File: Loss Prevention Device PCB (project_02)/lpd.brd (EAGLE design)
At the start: 160 x 100 mm, 5 parts, among them K1 LPPB041NGCN-RC, U1 POCKETBEAGLE, U2 GT-U7, U3 HM-10

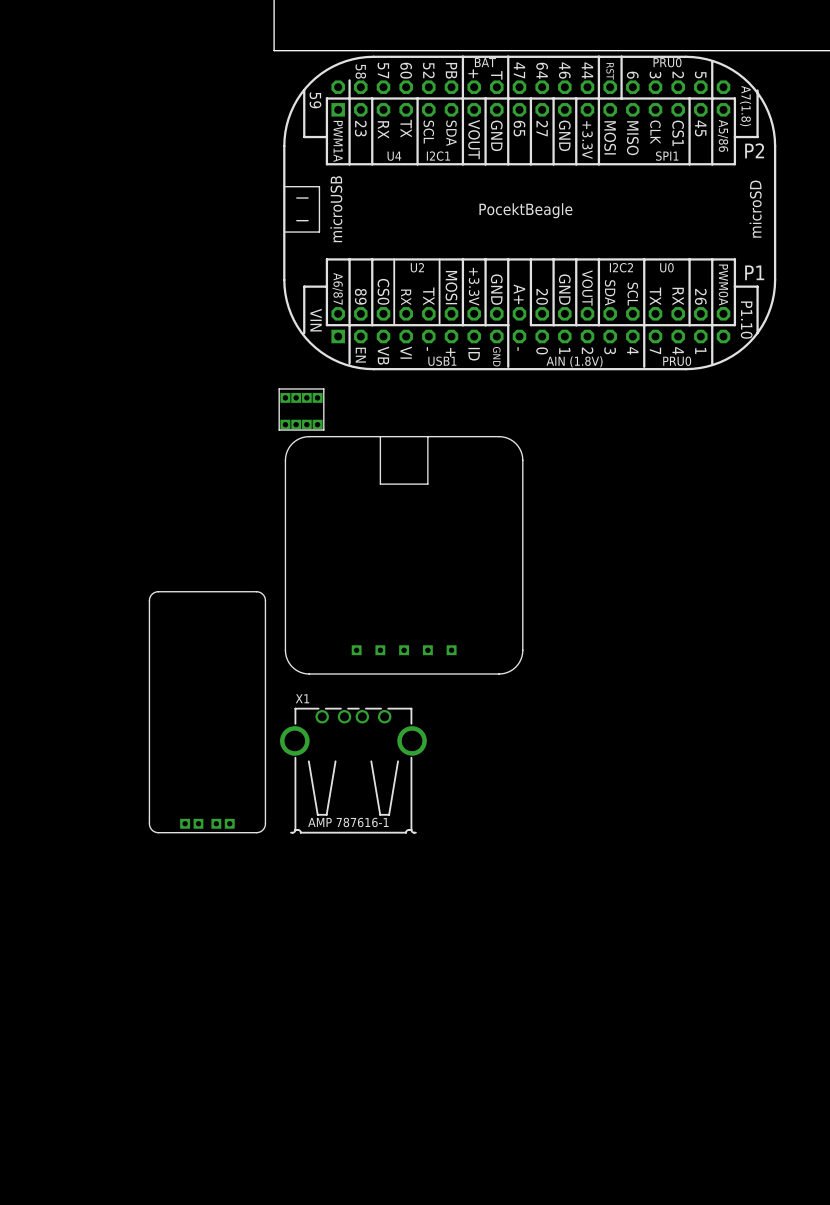
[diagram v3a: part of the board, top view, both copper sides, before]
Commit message: Split pocketbeagle symbol into 2
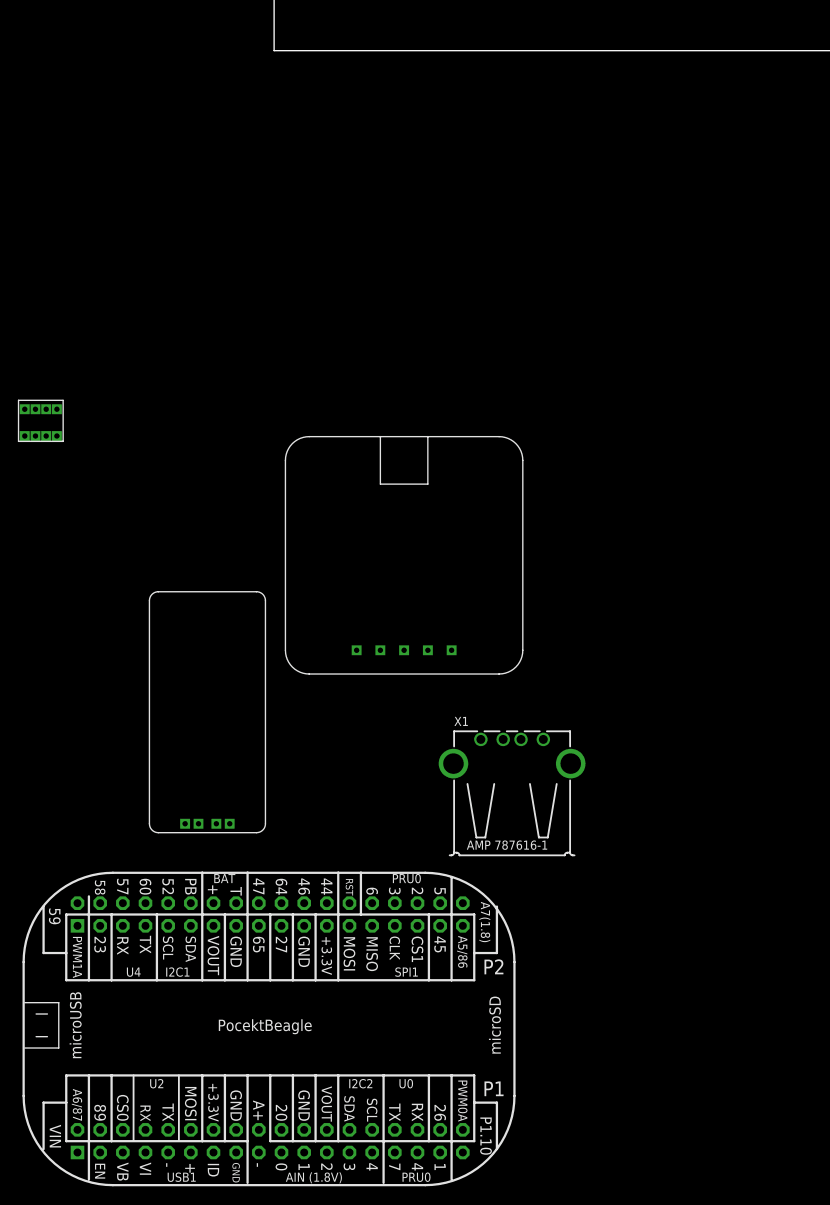
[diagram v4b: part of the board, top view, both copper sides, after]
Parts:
- removed U1: POCKETBEAGLE, lpd:POCKETBEAGLE
- added U$1: POCKETBEAGLE, lpd:POCKETBEAGLE
- moved K1 29.2 mm to (-27.9, -43.2)
- moved X1 18.0 mm to (26.7, -90.2)
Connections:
- removed net USB1.GND: X1.4
- net BAT.VIN: now also U$1.P1_12; no longer U1.P2_14
- net GND: now also U$1.P2_22, U$1.P2_23, U$1.P2_24, U$1.P2_25, U$1.P2_26, X1.4; no longer U1.P1_15, U1.P1_16, U1.P1_22, U1.P2_15, U1.P2_21
- net UART2.RX: now also U$1.P2_27; no longer U1.P1_08
- net UART2.TX: now also U$1.P2_28; no longer U1.P1_10
- net UART4.RX: now also U$1.P2_29; no longer U1.P2_05
- net UART4.TX: now also U$1.P2_30; no longer U1.P2_07
- net USB1.D+: now also U$1.P2_31; no longer U1.P1_11
- net USB1.D-: now also U$1.P2_32; no longer U1.P1_09
- net USB1.VBUS: now also U$1.P2_35; no longer U1.P1_05
- net VDD_3P3V: now also U$1.P2_20, U$1.P2_21; no longer U1.P1_14, U1.P2_23
- net VIN: now also U$1.P2_17; no longer U1.P1_01
- net VOUT: now also U$1.P2_18, U$1.P2_19; no longer U1.P1_24, U1.P2_13
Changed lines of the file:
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@@
 </autorouter>
 <elements>
-<element name="U1" library="lpd" package="POCKETBEAGLE" value="POCKETBEAGLE" x="1.27" y="-35.56" smashed="yes"/>
-<element name="K1" library="lpd" package="FEMALE90" value="LPPB041NGCN-RC" x="1.27" y="-41.91" smashed="yes"/>
+<element name="K1" library="lpd" package="FEMALE90" value="LPPB041NGCN-RC" x="-27.94" y="-43.18" smashed="yes"/>
 <element name="U2" library="lpd" package="GPS" value="GT-U7" x="1.27" y="-69.85" smashed="yes"/>
-<element name="X1" library="lpd" package="GHI2_USB_HOST_HORIZONTAL_W/CHASSIS_GND" value="" x="8.89" y="-87.63" smashed="yes">
-<attribute name="NAME" x="2.3899" y="-73.1299" size="1.016" layer="25" ratio="12"/>
-<attribute name="VALUE" x="4.3899" y="-77.63" size="1.016" layer="27" ratio="12"/>
+<element name="X1" library="lpd" package="GHI2_USB_HOST_HORIZONTAL_W/CHASSIS_GND" value="" x="26.67" y="-90.17" smashed="yes">
+<attribute name="NAME" x="20.1699" y="-75.6699" size="1.016" layer="25" ratio="12"/>
+<attribute name="VALUE" x="22.1699" y="-80.17" size="1.016" layer="27" ratio="12"/>
 </element>
 <element name="U3" library="lpd" package="BT" value="HM-10" x="-13.97" y="-87.63" smashed="yes"/>
+<element name="U$1" library="lpd" package="POCKETBEAGLE" value="POCKETBEAGLE" x="-27.94" y="-127" smashed="yes"/>
 </elements>
 <signals>
-<signal name="VIN">
-<contactref element="U1" pad="P1_01"/>
-</signal>
 <signal name="GND">
-<contactref element="U1" pad="P1_22"/>
-<contactref element="U1" pad="P2_21"/>
 <contactref element="U2" pad="P$1"/>
 <contactref element="K1" pad="P$2"/>
-<contactref element="U1" pad="P1_15"/>
-<contactref element="U1" pad="P1_16"/>
-<contactref element="U1" pad="P2_15"/>
-<wire x1="2.47" y1="-41.91" x2="9.25" y2="-67.19" width="0" layer="19" extent="1-1"/>
-<wire x1="24.96" y1="-32.03" x2="2.47" y2="-41.91" width="0" layer="19" extent="1-1"/>
-<wire x1="24.96" y1="-29.49" x2="24.96" y2="-32.03" width="0" layer="19" extent="1-1"/>
-<wire x1="32.58" y1="-29.49" x2="24.96" y2="-29.49" width="0" layer="19" extent="1-1"/>
-<wire x1="32.58" y1="-6.63" x2="32.58" y2="-29.49" width="0" layer="19" extent="1-1"/>
-<wire x1="24.96" y1="-6.63" x2="32.58" y2="-6.63" width="0" layer="19" extent="1-1"/>
-</signal>
-<signal name="VOUT">
-<contactref element="U1" pad="P1_24"/>
-<contactref element="U1" pad="P2_13"/>
-<wire x1="35.12" y1="-29.49" x2="22.42" y2="-6.63" width="0" layer="19" extent="1-1"/>
-</signal>
-<signal name="BAT.VIN">
-<contactref element="U1" pad="P2_14"/>
+<contactref element="X1" pad="4"/>
+<contactref element="U$1" pad="P2_23"/>
+<contactref element="U$1" pad="P2_24"/>
+<contactref element="U$1" pad="P2_25"/>
+<contactref element="U$1" pad="P2_26"/>
+<contactref element="U$1" pad="P2_22"/>
+<wire x1="5.91" y1="-95.53" x2="5.91" y2="-98.07" width="0" layer="19" extent="1-1"/>
+<wire x1="3.37" y1="-95.53" x2="5.91" y2="-95.53" width="0" layer="19" extent="1-1"/>
+<wire x1="8.45" y1="-98.07" x2="5.91" y2="-98.07" width="0" layer="19" extent="1-1"/>
+<wire x1="8.45" y1="-95.53" x2="5.91" y2="-95.53" width="0" layer="19" extent="1-1"/>
+<wire x1="9.25" y1="-67.19" x2="8.45" y2="-95.53" width="0" layer="19" extent="1-1"/>
+<wire x1="30.17" y1="-77.18" x2="9.25" y2="-67.19" width="0" layer="19" extent="1-1"/>
+<wire x1="-26.74" y1="-43.18" x2="9.25" y2="-67.19" width="0" layer="19" extent="1-1"/>
 </signal>
 <signal name="VDD_3P3V">
-<contactref element="U1" pad="P2_23"/>
-<contactref element="U1" pad="P1_14"/>
 <contactref element="U2" pad="P$5"/>
 <contactref element="K1" pad="P$1"/>
-<wire x1="1.27" y1="-41.91" x2="19.89" y2="-67.19" width="0" layer="19" extent="1-1"/>
-<wire x1="22.42" y1="-29.49" x2="1.27" y2="-41.91" width="0" layer="19" extent="1-1"/>
-<wire x1="35.12" y1="-6.63" x2="22.42" y2="-29.49" width="0" layer="19" extent="1-1"/>
+<contactref element="U$1" pad="P2_21"/>
+<contactref element="U$1" pad="P2_20"/>
+<wire x1="0.83" y1="-95.53" x2="3.37" y2="-98.07" width="0" layer="19" extent="1-1"/>
+<wire x1="19.89" y1="-67.19" x2="0.83" y2="-95.53" width="0" layer="19" extent="1-1"/>
+<wire x1="-27.94" y1="-43.18" x2="19.89" y2="-67.19" width="0" layer="19" extent="1-1"/>
 </signal>
 <signal name="UART2.RX">
 <contactref element="U2" pad="P$3"/>
-<contactref element="U1" pad="P1_08"/>
-<wire x1="14.8" y1="-29.49" x2="14.57" y2="-67.19" width="0" layer="19" extent="1-1"/>
+<contactref element="U$1" pad="P2_27"/>
+<wire x1="14.57" y1="-67.19" x2="10.99" y2="-98.07" width="0" layer="19" extent="1-1"/>
 </signal>
 <signal name="UART2.TX">
 <contactref element="U2" pad="P$4"/>
-<contactref element="U1" pad="P1_10"/>
-<wire x1="17.34" y1="-29.49" x2="17.23" y2="-67.19" width="0" layer="19" extent="1-1"/>
+<contactref element="U$1" pad="P2_28"/>
+<wire x1="17.23" y1="-67.19" x2="10.99" y2="-95.53" width="0" layer="19" extent="1-1"/>
 </signal>
 <signal name="UART4.TX">
 <contactref element="K1" pad="P$3"/>
-<contactref element="U1" pad="P2_07"/>
-<wire x1="14.8" y1="-6.63" x2="3.67" y2="-41.91" width="0" layer="19" extent="1-1"/>
+<contactref element="U$1" pad="P2_30"/>
+<wire x1="-25.54" y1="-43.18" x2="13.53" y2="-95.53" width="0" layer="19" extent="1-1"/>
 </signal>
 <signal name="UART4.RX">
 <contactref element="K1" pad="P$4"/>
-<contactref element="U1" pad="P2_05"/>
-<wire x1="12.26" y1="-6.63" x2="4.87" y2="-41.91" width="0" layer="19" extent="1-1"/>
+<contactref element="U$1" pad="P2_29"/>
+<wire x1="-24.34" y1="-43.18" x2="13.53" y2="-98.07" width="0" layer="19" extent="1-1"/>
 </signal>
 <signal name="ANGLE1">
 <contactref element="K1" pad="P$5"/>
 <contactref element="U3" pad="P$4"/>
-<wire x1="1.27" y1="-38.91" x2="-4.97" y2="-86.63" width="0" layer="19" extent="1-1"/>
+<wire x1="-27.94" y1="-40.18" x2="-4.97" y2="-86.63" width="0" layer="19" extent="1-1"/>
 </signal>
 <signal name="ANGLE2">
 <contactref element="K1" pad="P$6"/>
 <contactref element="U3" pad="P$1"/>
-<wire x1="2.47" y1="-38.91" x2="-9.97" y2="-86.63" width="0" layer="19" extent="1-1"/>
+<wire x1="-26.74" y1="-40.18" x2="-9.97" y2="-86.63" width="0" layer="19" extent="1-1"/>
 </signal>
 <signal name="ANGLE3">
 <contactref element="K1" pad="P$7"/>
 <contactref element="U3" pad="P$3"/>
-<wire x1="3.67" y1="-38.91" x2="-6.47" y2="-86.63" width="0" layer="19" extent="1-1"/>
+<wire x1="-25.54" y1="-40.18" x2="-6.47" y2="-86.63" width="0" layer="19" extent="1-1"/>
 </signal>
 <signal name="ANGLE4">
 <contactref element="K1" pad="P$8"/>
 <contactref element="U3" pad="P$2"/>
-<wire x1="4.87" y1="-38.91" x2="-8.47" y2="-86.63" width="0" layer="19" extent="1-1"/>
+<wire x1="-24.34" y1="-40.18" x2="-8.47" y2="-86.63" width="0" layer="19" extent="1-1"/>
 </signal>
 <signal name="CGND">
 <contactref element="X1" pad="5"/>
 <contactref element="X1" pad="6"/>
-<wire x1="15.46" y1="-77.3501" x2="2.32" y2="-77.3501" width="0" layer="19" extent="1-1"/>
+<wire x1="33.24" y1="-79.8901" x2="20.1" y2="-79.8901" width="0" layer="19" extent="1-1"/>
 </signal>
 <signal name="USB1.VBUS">
 <contactref element="X1" pad="1"/>
-<contactref element="U1" pad="P1_05"/>
-<wire x1="12.26" y1="-32.03" x2="5.39" y2="-74.64" width="0" layer="19" extent="1-1"/>
+<contactref element="U$1" pad="P2_35"/>
+<wire x1="23.17" y1="-77.18" x2="21.15" y2="-98.07" width="0" layer="19" extent="1-1"/>
 </signal>
 <signal name="USB1.D-">
 <contactref element="X1" pad="2"/>
-<contactref element="U1" pad="P1_09"/>
-<wire x1="17.34" y1="-32.03" x2="7.89" y2="-74.64" width="0" layer="19" extent="1-1"/>
+<contactref element="U$1" pad="P2_32"/>
+<wire x1="25.67" y1="-77.18" x2="16.07" y2="-95.53" width="0" layer="19" extent="1-1"/>
 </signal>
 <signal name="USB1.D+">
 <contactref element="X1" pad="3"/>
-<contactref element="U1" pad="P1_11"/>
-<wire x1="19.88" y1="-32.03" x2="9.89" y2="-74.64" width="0" layer="19" extent="1-1"/>
+<contactref element="U$1" pad="P2_31"/>
+<wire x1="27.67" y1="-77.18" x2="16.07" y2="-98.07" width="0" layer="19" extent="1-1"/>
 </signal>
-<signal name="USB1.GND">
-<contactref element="X1" pad="4"/>
+<signal name="VIN">
+<contactref element="U$1" pad="P2_17"/>
+</signal>
+<signal name="VOUT">
+<contactref element="U$1" pad="P2_18"/>
+<contactref element="U$1" pad="P2_19"/>
+<wire x1="-1.71" y1="-95.53" x2="0.83" y2="-98.07" width="0" layer="19" extent="1-1"/>
+</signal>
+<signal name="BAT.VIN">
+<contactref element="U$1" pad="P1_12"/>
 </signal>
 </signals>

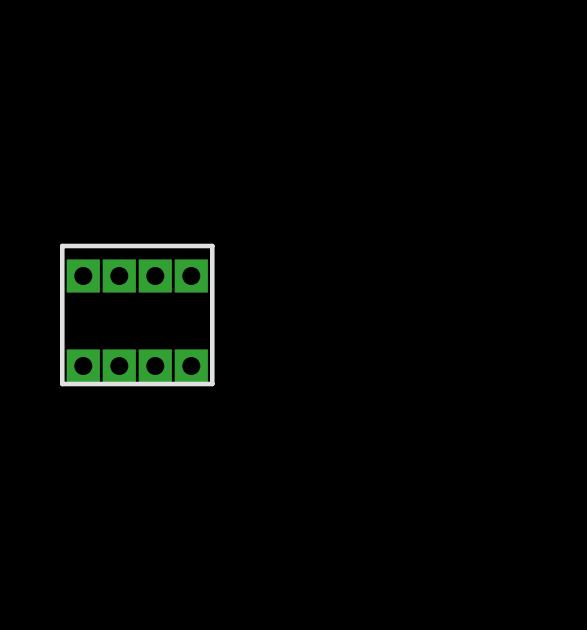
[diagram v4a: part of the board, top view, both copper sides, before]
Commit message: Removed 90 degree header and updated footprints
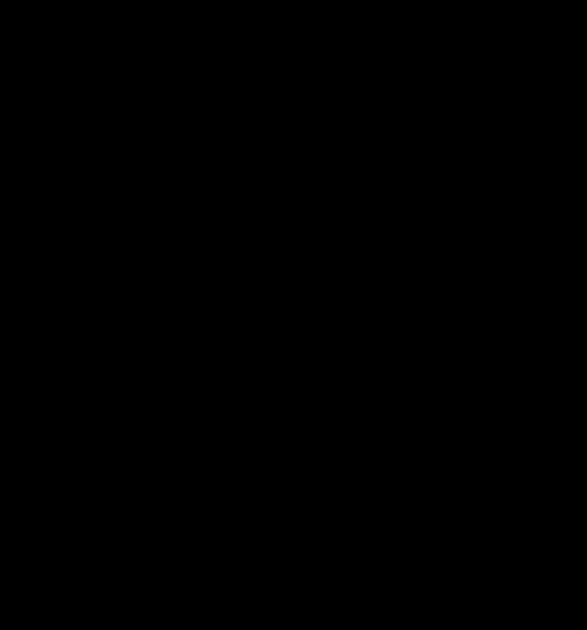
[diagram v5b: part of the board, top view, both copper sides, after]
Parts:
- removed K1: LPPB041NGCN-RC, lpd:FEMALE90
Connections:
- removed net ANGLE1: K1.P$5, U3.P$4
- removed net ANGLE2: K1.P$6, U3.P$1
- removed net ANGLE3: K1.P$7, U3.P$3
- removed net ANGLE4: K1.P$8, U3.P$2
- net GND: now also U3.P$1; no longer K1.P$2
- net UART4.RX: now also U3.P$2; no longer K1.P$4
- net UART4.TX: now also U3.P$3; no longer K1.P$3
- net VDD_3P3V: now also U3.P$4; no longer K1.P$1
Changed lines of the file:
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@@
 </autorouter>
 <elements>
-<element name="K1" library="lpd" package="FEMALE90" value="LPPB041NGCN-RC" x="-27.94" y="-43.18" smashed="yes"/>
 <element name="U2" library="lpd" package="GPS" value="GT-U7" x="1.27" y="-69.85" smashed="yes"/>
 <element name="X1" library="lpd" package="GHI2_USB_HOST_HORIZONTAL_W/CHASSIS_GND" value="" x="26.67" y="-90.17" smashed="yes">
@@
 <signal name="GND">
 <contactref element="U2" pad="P$1"/>
-<contactref element="K1" pad="P$2"/>
 <contactref element="X1" pad="4"/>
 <contactref element="U$1" pad="P2_23"/>
@@
 <contactref element="U$1" pad="P2_26"/>
 <contactref element="U$1" pad="P2_22"/>
-<wire x1="5.91" y1="-95.53" x2="5.91" y2="-98.07" width="0" layer="19" extent="1-1"/>
-<wire x1="3.37" y1="-95.53" x2="5.91" y2="-95.53" width="0" layer="19" extent="1-1"/>
+<contactref element="U3" pad="P$1"/>
+<wire x1="3.37" y1="-95.53" x2="-9.97" y2="-86.63" width="0" layer="19" extent="1-1"/>
+<wire x1="5.91" y1="-95.53" x2="3.37" y2="-95.53" width="0" layer="19" extent="1-1"/>
+<wire x1="5.91" y1="-98.07" x2="5.91" y2="-95.53" width="0" layer="19" extent="1-1"/>
 <wire x1="8.45" y1="-98.07" x2="5.91" y2="-98.07" width="0" layer="19" extent="1-1"/>
 <wire x1="8.45" y1="-95.53" x2="5.91" y2="-95.53" width="0" layer="19" extent="1-1"/>
-<wire x1="9.25" y1="-67.19" x2="8.45" y2="-95.53" width="0" layer="19" extent="1-1"/>
+<wire x1="9.25" y1="-67.19" x2="-9.97" y2="-86.63" width="0" layer="19" extent="1-1"/>
 <wire x1="30.17" y1="-77.18" x2="9.25" y2="-67.19" width="0" layer="19" extent="1-1"/>
-<wire x1="-26.74" y1="-43.18" x2="9.25" y2="-67.19" width="0" layer="19" extent="1-1"/>
 </signal>
 <signal name="VDD_3P3V">
 <contactref element="U2" pad="P$5"/>
-<contactref element="K1" pad="P$1"/>
 <contactref element="U$1" pad="P2_21"/>
 <contactref element="U$1" pad="P2_20"/>
+<contactref element="U3" pad="P$4"/>
 <wire x1="0.83" y1="-95.53" x2="3.37" y2="-98.07" width="0" layer="19" extent="1-1"/>
-<wire x1="19.89" y1="-67.19" x2="0.83" y2="-95.53" width="0" layer="19" extent="1-1"/>
-<wire x1="-27.94" y1="-43.18" x2="19.89" y2="-67.19" width="0" layer="19" extent="1-1"/>
+<wire x1="-4.97" y1="-86.63" x2="0.83" y2="-95.53" width="0" layer="19" extent="1-1"/>
+<wire x1="19.89" y1="-67.19" x2="-4.97" y2="-86.63" width="0" layer="19" extent="1-1"/>
 </signal>
 <signal name="UART2.RX">
@@
 </signal>
 <signal name="UART4.TX">
-<contactref element="K1" pad="P$3"/>
 <contactref element="U$1" pad="P2_30"/>
-<wire x1="-25.54" y1="-43.18" x2="13.53" y2="-95.53" width="0" layer="19" extent="1-1"/>
+<contactref element="U3" pad="P$3"/>
+<wire x1="13.53" y1="-95.53" x2="-6.47" y2="-86.63" width="0" layer="19" extent="1-1"/>
 </signal>
 <signal name="UART4.RX">
-<contactref element="K1" pad="P$4"/>
 <contactref element="U$1" pad="P2_29"/>
-<wire x1="-24.34" y1="-43.18" x2="13.53" y2="-98.07" width="0" layer="19" extent="1-1"/>
-</signal>
-<signal name="ANGLE1">
-<contactref element="K1" pad="P$5"/>
-<contactref element="U3" pad="P$4"/>
-<wire x1="-27.94" y1="-40.18" x2="-4.97" y2="-86.63" width="0" layer="19" extent="1-1"/>
-</signal>
-<signal name="ANGLE2">
-<contactref element="K1" pad="P$6"/>
-<contactref element="U3" pad="P$1"/>
-<wire x1="-26.74" y1="-40.18" x2="-9.97" y2="-86.63" width="0" layer="19" extent="1-1"/>
-</signal>
-<signal name="ANGLE3">
-<contactref element="K1" pad="P$7"/>
-<contactref element="U3" pad="P$3"/>
-<wire x1="-25.54" y1="-40.18" x2="-6.47" y2="-86.63" width="0" layer="19" extent="1-1"/>
-</signal>
-<signal name="ANGLE4">
-<contactref element="K1" pad="P$8"/>
 <contactref element="U3" pad="P$2"/>
-<wire x1="-24.34" y1="-40.18" x2="-8.47" y2="-86.63" width="0" layer="19" extent="1-1"/>
+<wire x1="13.53" y1="-98.07" x2="-8.47" y2="-86.63" width="0" layer="19" extent="1-1"/>
 </signal>
 <signal name="CGND">

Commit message: Board Placement Complete
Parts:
- moved U$1 144.3 mm to (38.1, 1.27), turned to 90 degrees
- moved U3 102.2 mm to (31.8, 3.81)
- moved U2 101.6 mm to (2.54, 31.8)
- moved X1 91.7 mm to (20.3, 1.27)
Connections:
- net BAT.VIN: now also U$1.P1_25; no longer U$1.P1_12
- net GND: now also U$1.P1_15, U$1.P1_16, U$1.P1_22, U$1.P2_15, U$1.P2_21; no longer U$1.P2_22, U$1.P2_23, U$1.P2_24, U$1.P2_25, U$1.P2_26
- net UART2.RX: now also U$1.P1_08; no longer U$1.P2_27
- net UART2.TX: now also U$1.P1_10; no longer U$1.P2_28
- net UART4.RX: now also U$1.P2_05; no longer U$1.P2_29
- net UART4.TX: now also U$1.P2_07; no longer U$1.P2_30
- net USB1.D+: now also U$1.P1_11; no longer U$1.P2_31
- net USB1.D-: now also U$1.P1_09; no longer U$1.P2_32
- net USB1.VBUS: now also U$1.P1_05; no longer U$1.P2_35
- net VDD_3P3V: now also U$1.P1_14, U$1.P1_23; no longer U$1.P2_20, U$1.P2_21
- net VIN: now also U$1.P2_34; no longer U$1.P2_17
- net VOUT: now also U$1.P2_35, U$1.P2_36; no longer U$1.P2_18, U$1.P2_19
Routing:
- added copper zone on layer 2, net GND
- added copper zone on layer 15, net VDD_3P3V
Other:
- board size 160 x 100 mm -> 48.3 x 58.4 mm

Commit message: Routing
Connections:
- removed net CGND: X1.5, X1.6
- net GND: now also X1.5, X1.6
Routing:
- net USB1.D-: track 0.00 -> 61.6 mm
- net USB1.D+: track 0.00 -> 54.9 mm
- net UART4.TX: track 0.00 -> 38.5 mm
- net UART4.RX: track 0.00 -> 34.6 mm
- net UART2.RX: track 0.00 -> 27.2 mm
- net UART2.TX: track 0.00 -> 23.5 mm
- net USB1.VBUS: track 0.00 -> 19.6 mm
